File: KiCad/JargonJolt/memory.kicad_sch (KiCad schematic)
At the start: 0 parts

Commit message: worked on schematic
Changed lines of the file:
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@@
 (kicad_sch (version 20230121) (generator eeschema)
   (paper "A4")
-  (hierarchical_label "VSPI_MOSI" (shape input) (at 33.401 48.641 180) (fields_autoplaced)
+  (hierarchical_label "MOSI" (shape input) (at 33.401 48.641 180) (fields_autoplaced)
     (effects (font (size 1.27 1.27)) (justify right))
   )
-  (hierarchical_label "VSPI_SCLK" (shape input) (at 33.528 58.293 180) (fields_autoplaced)
+  (hierarchical_label "SCLK" (shape input) (at 33.528 58.293 180) (fields_autoplaced)
     (effects (font (size 1.27 1.27)) (justify right))
   )
-  (hierarchical_label "VSPI_MISO" (shape input) (at 33.528 45.72 180) (fields_autoplaced)
+  (hierarchical_label "MISO" (shape input) (at 33.528 45.72 180) (fields_autoplaced)
     (effects (font (size 1.27 1.27)) (justify right))
   )
-  (hierarchical_label "VSPI_CS2" (shape input) (at 33.655 51.816 180) (fields_autoplaced)
+  (hierarchical_label "CS2" (shape input) (at 33.655 51.816 180) (fields_autoplaced)
     (effects (font (size 1.27 1.27)) (justify right))
   )
-  (hierarchical_label "VSPI_CS1" (shape input) (at 33.655 55.499 180) (fields_autoplaced)
+  (hierarchical_label "CS1" (shape input) (at 33.655 55.499 180) (fields_autoplaced)
     (effects (font (size 1.27 1.27)) (justify right))
   )

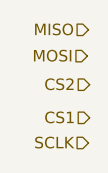
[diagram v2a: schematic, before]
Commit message: added i2s schematic
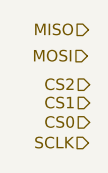
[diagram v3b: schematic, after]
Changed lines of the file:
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@@
+    (effects (font (size 1.27 1.27)) (justify right))
+  )
+  (hierarchical_label "CS0" (shape input) (at 33.655 56.007 180) (fields_autoplaced)
     (effects (font (size 1.27 1.27)) (justify right))
   )
@@
     (effects (font (size 1.27 1.27)) (justify right))
   )
-  (hierarchical_label "CS1" (shape input) (at 33.655 55.499 180) (fields_autoplaced)
+  (hierarchical_label "CS1" (shape input) (at 33.655 53.848 180) (fields_autoplaced)
     (effects (font (size 1.27 1.27)) (justify right))
   )

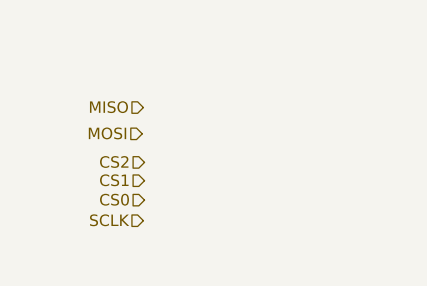
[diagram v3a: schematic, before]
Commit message: added sd module + fixed CS pins
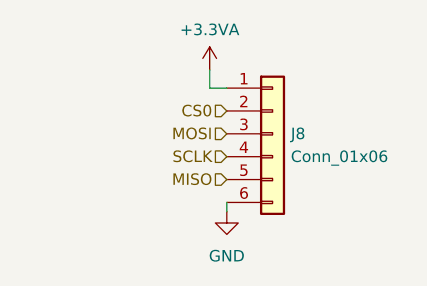
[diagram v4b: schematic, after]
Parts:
- added J8: Conn_01x06, symbol Connector_Generic:Conn_01x06
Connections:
- net CS0: now also J8.2 (Pin_2)
- net MISO: now also J8.5 (Pin_5)
- net MOSI: now also J8.3 (Pin_3)
- net SCLK: now also J8.4 (Pin_4)
- new net +3.3VA: J8.1 (Pin_1)
- new net GND: J8.6 (Pin_6)
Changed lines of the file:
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@@
 (kicad_sch (version 20230121) (generator eeschema)
   (paper "A4")
-  (hierarchical_label "MOSI" (shape input) (at 33.401 48.641 180) (fields_autoplaced)
+  (wire (pts (xy 40.894 41.529) (xy 40.894 43.561))
+    (stroke (width 0) (type default))
+  )
+  (wire (pts (xy 42.799 56.261) (xy 42.799 57.277))
+    (stroke (width 0) (type default))
+  )
+  (wire (pts (xy 40.894 43.561) (xy 42.799 43.561))
+    (stroke (width 0) (type default))
+  )
+  (hierarchical_label "MOSI" (shape input) (at 42.799 48.641 180) (fields_autoplaced)
     (effects (font (size 1.27 1.27)) (justify right))
   )
-  (hierarchical_label "SCLK" (shape input) (at 33.528 58.293 180) (fields_autoplaced)
+  (hierarchical_label "SCLK" (shape input) (at 42.799 51.181 180) (fields_autoplaced)
     (effects (font (size 1.27 1.27)) (justify right))
   )
-  (hierarchical_label "CS0" (shape input) (at 33.655 56.007 180) (fields_autoplaced)
+  (hierarchical_label "CS0" (shape input) (at 42.799 46.101 180) (fields_autoplaced)
     (effects (font (size 1.27 1.27)) (justify right))
   )
-  (hierarchical_label "MISO" (shape input) (at 33.528 45.72 180) (fields_autoplaced)
+  (hierarchical_label "MISO" (shape input) (at 42.799 53.721 180) (fields_autoplaced)
     (effects (font (size 1.27 1.27)) (justify right))
   )
-  (hierarchical_label "CS2" (shape input) (at 33.655 51.816 180) (fields_autoplaced)
-    (effects (font (size 1.27 1.27)) (justify right))
+  (symbol (lib_id "Connector_Generic:Conn_01x06") (at 47.879 48.641 0) (unit 1)
+    (in_bom yes) (on_board yes) (dnp no) (fields_autoplaced)
+    (property "Reference" "J8" (at 49.911 48.641 0)
+      (effects (font (size 1.27 1.27)) (justify left))
+    )
+    (property "Value" "Conn_01x06" (at 49.911 51.181 0)
+      (effects (font (size 1.27 1.27)) (justify left))
+    )
+    (property "Footprint" "" (at 47.879 48.641 0)
+      (effects (font (size 1.27 1.27)) hide)
+    )
+    (property "Datasheet" "~" (at 47.879 48.641 0)
+      (effects (font (size 1.27 1.27)) hide)
+    )
+    (pin "6")
+    (pin "1")
+    (pin "5")
+    (pin "3")
+    (pin "2")
+    (pin "4")
+    (instances
+      (project "JargonJolt"
+        (path "/39fa52d1-bab8-41e3-aba2-e2f783adaf1f/9752bf8f-f974-45f7-9164-dbd42fc6da6b"
+          (reference "J8") (unit 1)
+        )
+      )
+    )
   )
-  (hierarchical_label "CS1" (shape input) (at 33.655 53.848 180) (fields_autoplaced)
-    (effects (font (size 1.27 1.27)) (justify right))
+  (symbol (lib_id "power:GND") (at 42.799 57.277 0) (unit 1)
+    (in_bom yes) (on_board yes) (dnp no) (fields_autoplaced)
+    (property "Reference" "#PWR042" (at 42.799 63.627 0)
+      (effects (font (size 1.27 1.27)) hide)
+    )
+    (property "Value" "GND" (at 42.799 62.23 0)
+      (effects (font (size 1.27 1.27)))
+    )
+    (property "Footprint" "" (at 42.799 57.277 0)
+      (effects (font (size 1.27 1.27)) hide)
+    )
+    (property "Datasheet" "" (at 42.799 57.277 0)
+      (effects (font (size 1.27 1.27)) hide)
+    )
+    (pin "1")
+    (instances
+      (project "JargonJolt"
+        (path "/39fa52d1-bab8-41e3-aba2-e2f783adaf1f/9752bf8f-f974-45f7-9164-dbd42fc6da6b"
+          (reference "#PWR042") (unit 1)
+        )
+      )
+    )
+  )
+  (symbol (lib_id "power:+3.3VA") (at 40.894 41.529 0) (unit 1)
+    (in_bom yes) (on_board yes) (dnp no) (fields_autoplaced)
+    (property "Reference" "#PWR041" (at 40.894 45.339 0)
+      (effects (font (size 1.27 1.27)) hide)
+    )
+    (property "Value" "+3.3VA" (at 40.894 37.084 0)
+      (effects (font (size 1.27 1.27)))
+    )
+    (property "Footprint" "" (at 40.894 41.529 0)
+      (effects (font (size 1.27 1.27)) hide)
+    )
+    (property "Datasheet" "" (at 40.894 41.529 0)
+      (effects (font (size 1.27 1.27)) hide)
+    )
+    (pin "1")
+    (instances
+      (project "JargonJolt"
+        (path "/39fa52d1-bab8-41e3-aba2-e2f783adaf1f/9752bf8f-f974-45f7-9164-dbd42fc6da6b"
+          (reference "#PWR041") (unit 1)
+        )
+      )
+    )
   )
 )

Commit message: added more footprints
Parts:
- J8: footprint (none) -> Connector_PinHeader_2.54mm:PinHeader_1x06_P2.54mm_Vertical
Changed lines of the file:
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@@
       (effects (font (size 1.27 1.27)) (justify left))
     )
-    (property "Footprint" "" (at 47.879 48.641 0)
+    (property "Footprint" "Connector_PinHeader_2.54mm:PinHeader_1x06_P2.54mm_Vertical" (at 47.879 48.641 0)
       (effects (font (size 1.27 1.27)) hide)
     )
